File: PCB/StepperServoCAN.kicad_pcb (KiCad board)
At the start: 4 copper layers, 56 x 43.2 mm, 156 parts, among them J1 CAR, J2 Debug, J3 Motor, J4 Conn_01x06, Q1 AO3401A, Q2 2N7002, Q3 AO3401A, SW1 Rst, SW2 Fcn>, SW3 Fcn>, U1 AH1806-W, U10 HT75xx-1-SOT89, U11 LV2842XLVDDCR, U2 STM32F103CBT6, U3 LMV321, U4 A4950E, U5 A4950E, U6 LMV321, U7 TLE5012B, U8 TMAG5170-Q1, U9 SN65HVD230, Y1 16Mhz 9pF

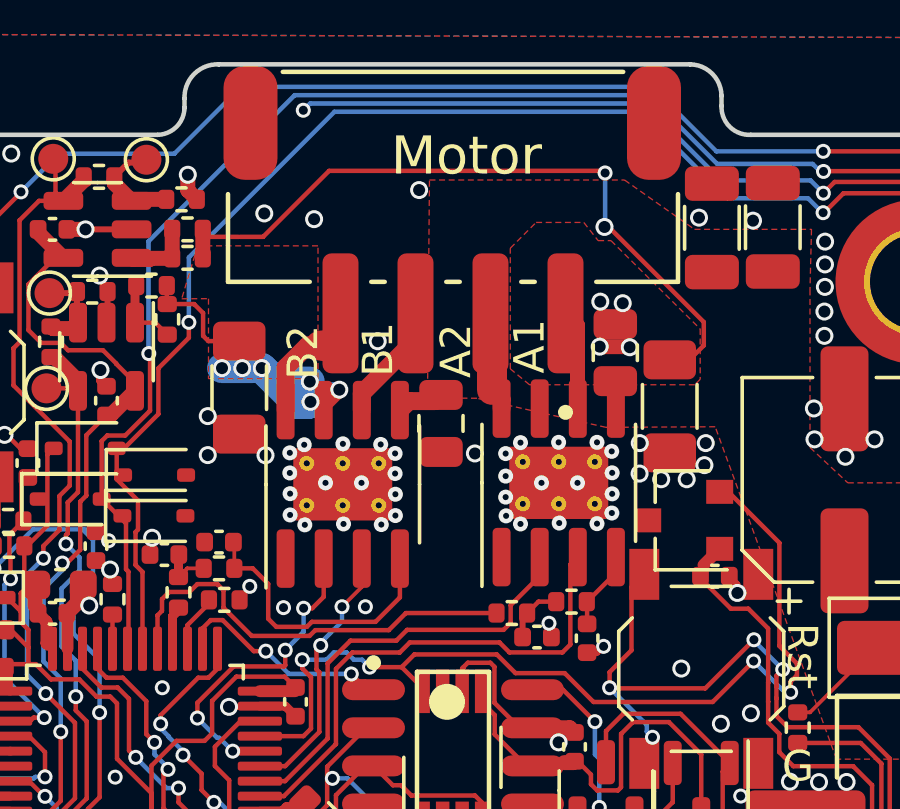
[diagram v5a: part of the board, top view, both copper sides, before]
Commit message: Bigger cap for B phase driver
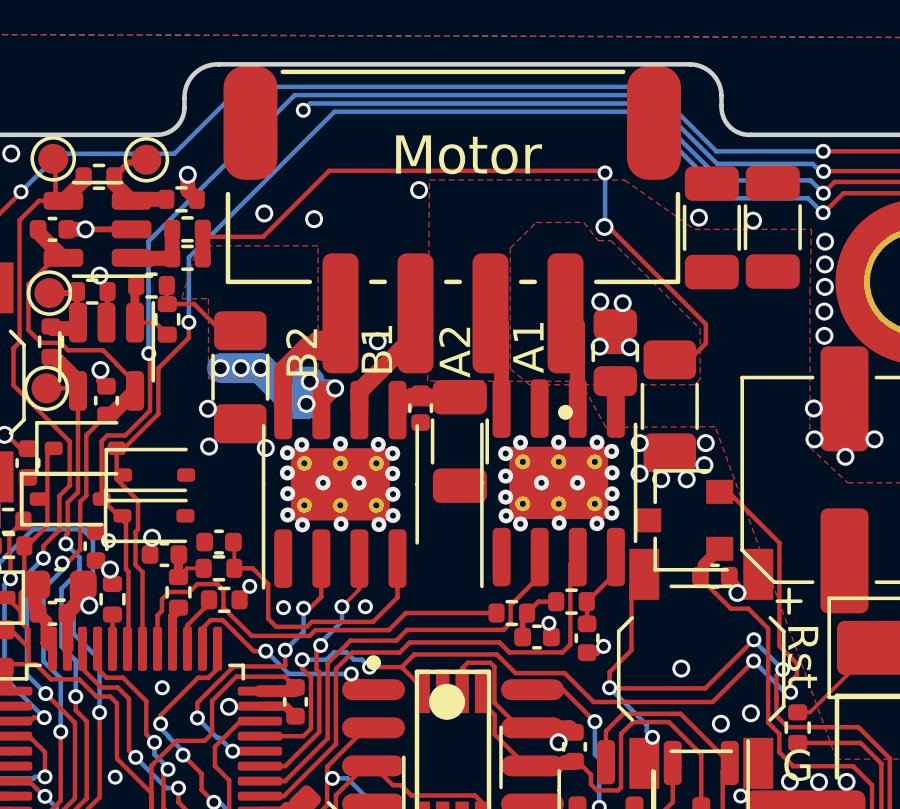
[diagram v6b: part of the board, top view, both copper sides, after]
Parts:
- added C29: 100n, Capacitor_SMD:C_0402_1005Metric, F.Cu at (98.9, 88.7)
- C23: value 1uF 50V -> 10u; footprint Capacitor_SMD:C_0805_2012Metric -> Capacitor_SMD:C_1206_3216Metric
- moved C23 0.87 mm to (100.2, 89.8)
- moved R32 0.35 mm to (92.9, 87.7)
- moved U5 0.08 mm to (96.2, 91.2)
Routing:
- net A4950_B_IN1: track 8.71 -> 9.62 mm
- net Motor_A2: track 2.91 -> 3.54 mm
- net GND: vias 162 -> 161

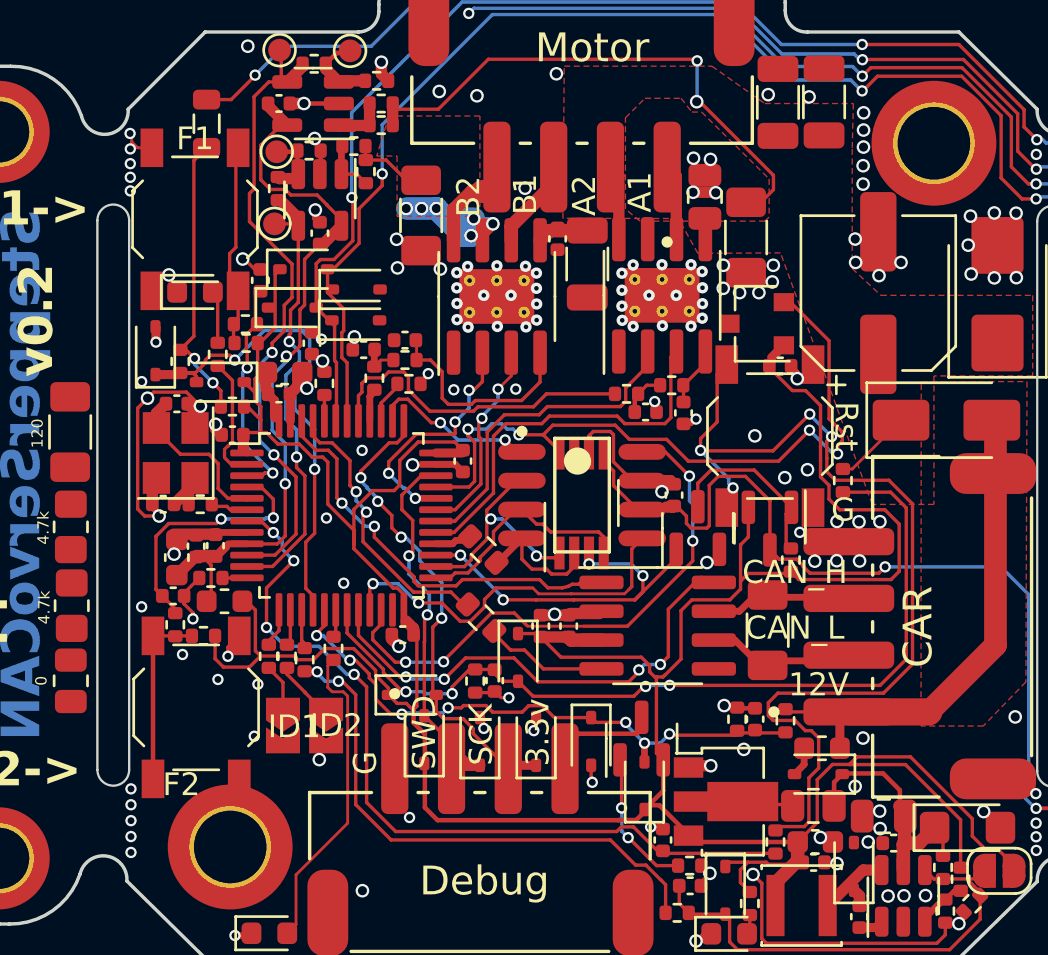
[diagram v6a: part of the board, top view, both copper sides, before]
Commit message: Crystal small ground guard ring
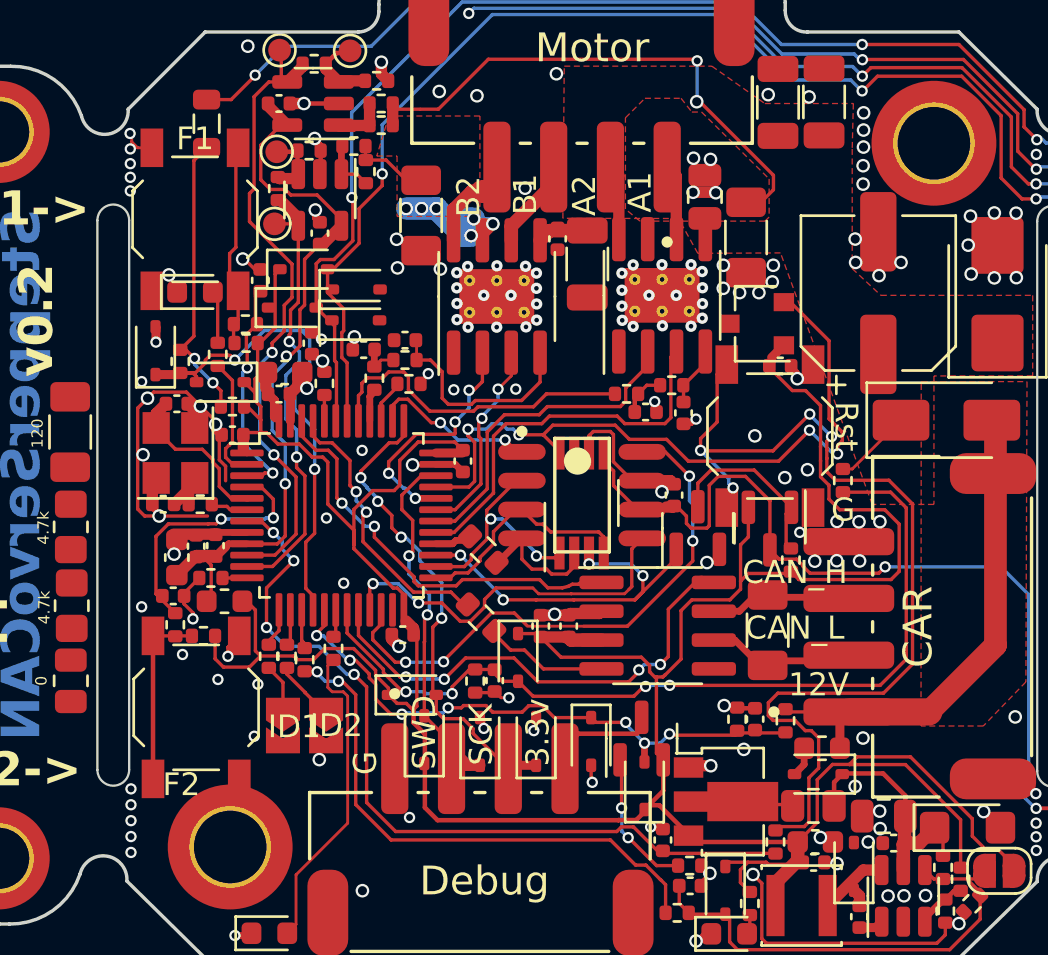
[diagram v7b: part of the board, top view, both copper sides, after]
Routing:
- net GND: track 125.9 -> 131.9 mm, vias 161 -> 162
- net LSS_B: track 11.2 -> 9.24 mm

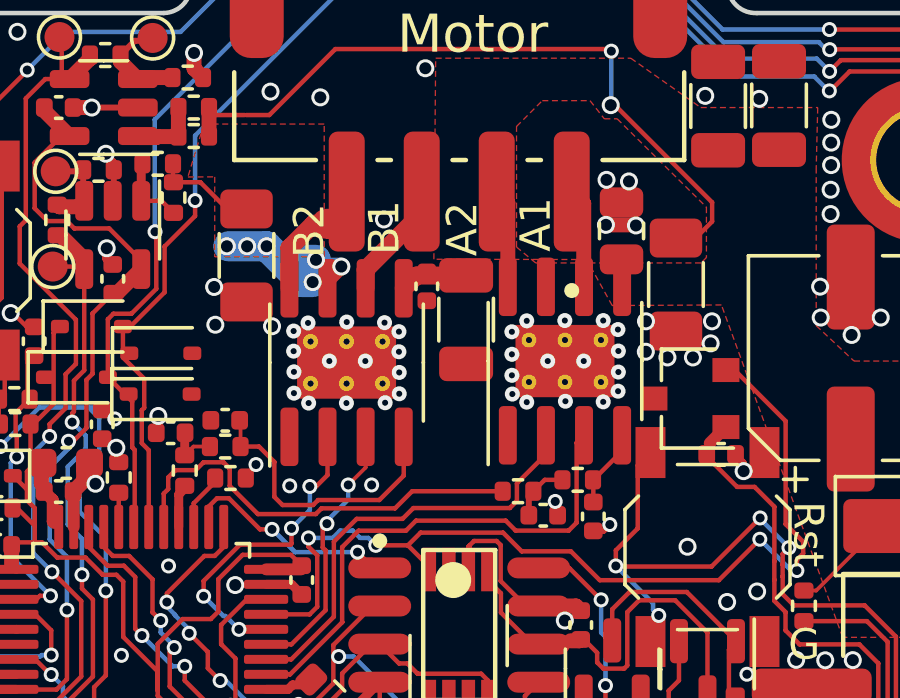
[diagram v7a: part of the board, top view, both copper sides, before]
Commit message: Lots of thermal vias. Resistors radiator.
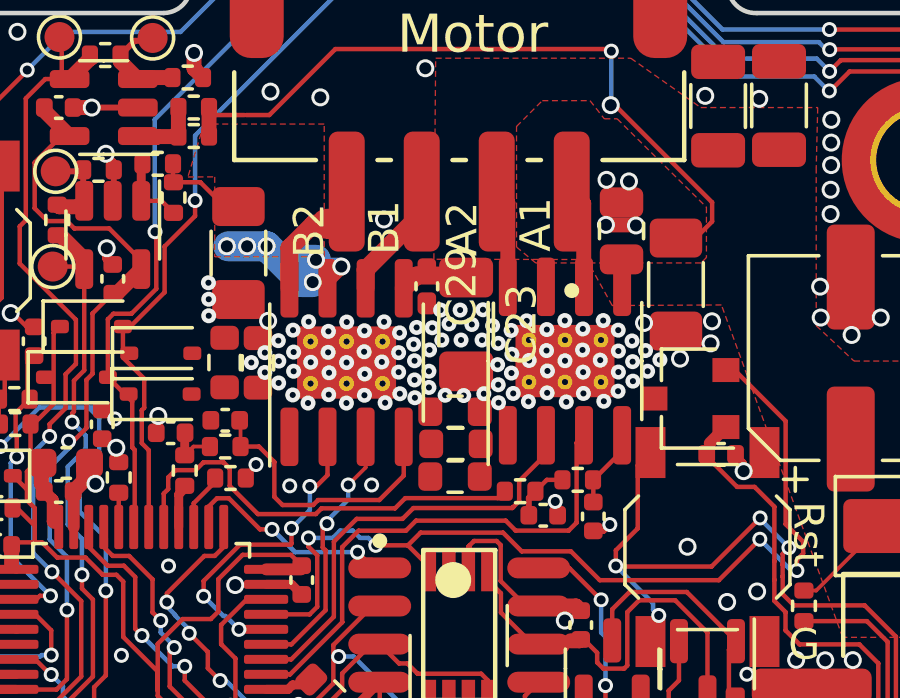
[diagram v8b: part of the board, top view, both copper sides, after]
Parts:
- added JP11: 0, Resistor_SMD:R_0603_1608Metric, F.Cu at (93.3, 91.3)
- added JP12: 0, Resistor_SMD:R_0603_1608Metric, F.Cu at (99.9, 94.0)
- added JP7: 0, Resistor_SMD:R_0603_1608Metric, F.Cu at (99.9, 92.9)
- added JP8: 0, Resistor_SMD:R_0603_1608Metric, F.Cu at (99.9, 95.0)
- added JP9: 0, Resistor_SMD:R_0603_1608Metric, F.Cu at (92.2, 91.2)
- C23: footprint Capacitor_SMD:C_1206_3216Metric -> Capacitor_SMD:C_1206_3216Metric_Pad1.33x1.80mm_HandSolder
- C28: value 1u -> 1u 25V
- C29: value 100n -> 100n 50V; footprint Capacitor_SMD:C_0402_1005Metric -> Capacitor_SMD:C_0402_1005Metric_Pad0.74x0.62mm_HandSolder
- moved R32 0.28 mm to (92.6, 87.6)
- moved C23 0.16 mm to (100.2, 90.0)
- moved R19 0.07 mm to (102.0, 95.5)
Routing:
- net VMOT: track 5.13 -> 5.73 mm
- net GND: vias 162 -> 216
